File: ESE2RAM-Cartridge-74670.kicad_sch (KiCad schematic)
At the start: 27 parts, among them IC1 4M SRAM, IC2 4M SRAM, J1 BUS_MSX, J2 8M, U1 74HC670, U2 74HC670, U3 74HC138, U4 74HC00, U5 74HC32

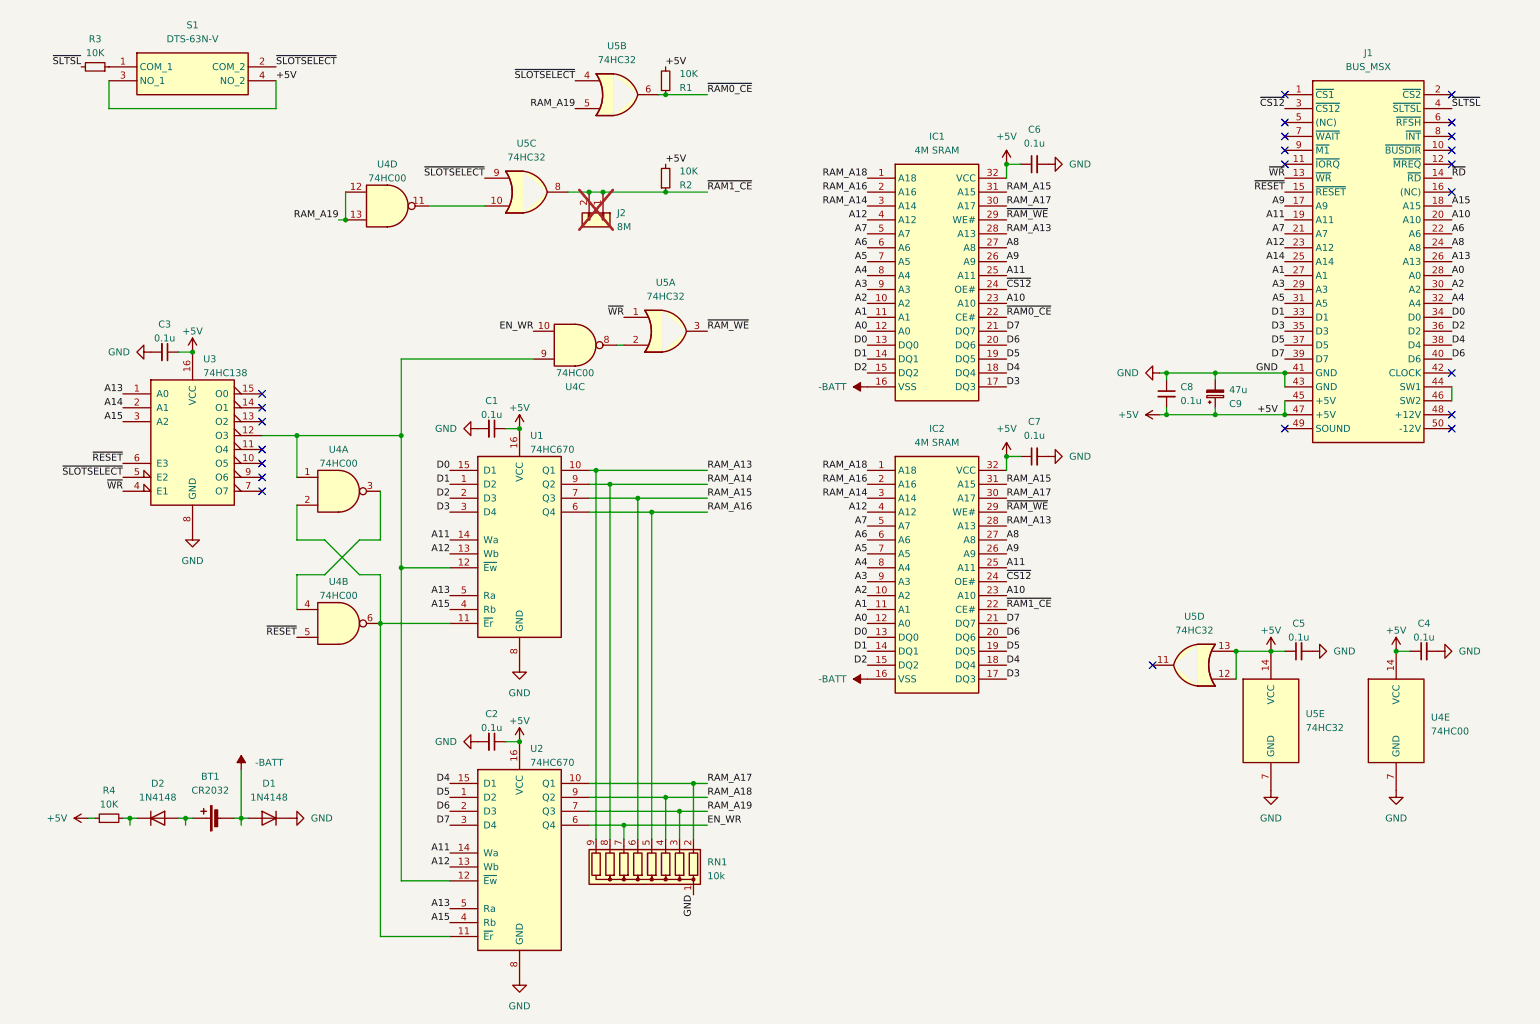
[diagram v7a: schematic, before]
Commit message: Modified Schematic
一部MSX機種での動作不良修正のため74HC00/74HC32/74HC138を74AHCシリーズに変更
Changed 74HC00/74HC32/74HC138 to 74AHC series to fix malfunction on some MSX models.
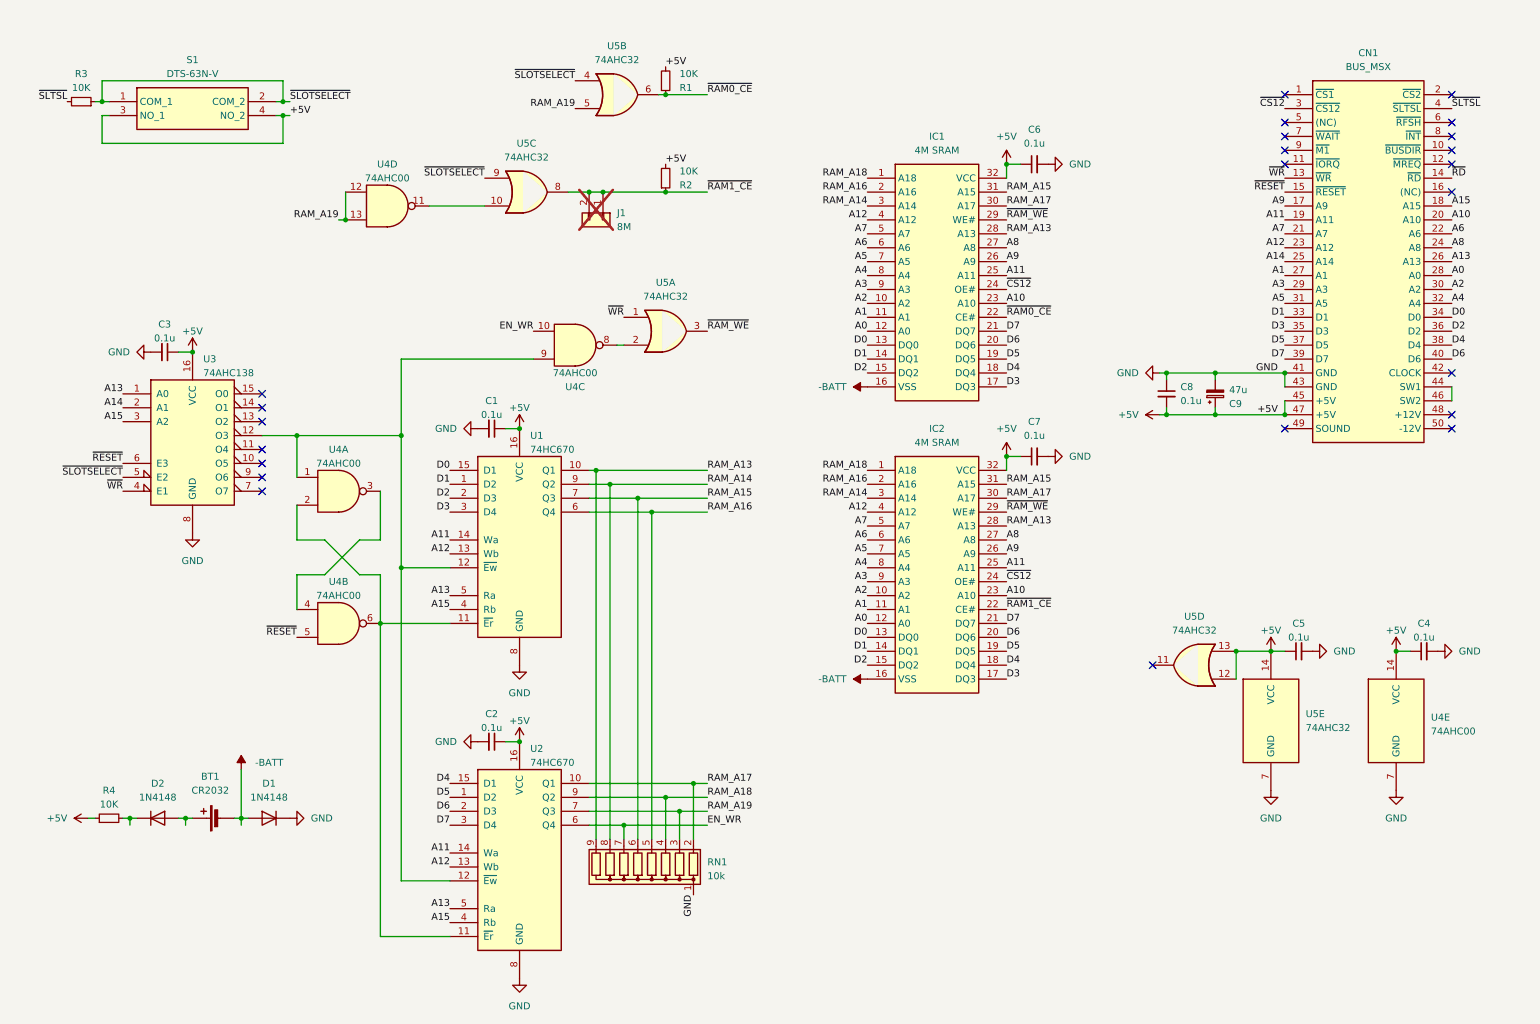
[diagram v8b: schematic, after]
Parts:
- U3: value 74HC138 -> 74AHC138
- U4: value 74HC00 -> 74AHC00
- U5: value 74HC32 -> 74AHC32
- renumbered J1 to CN1, J2 to J1
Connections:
- net ~{SLOTSELECT}: now also R3.1, S1.1 (COM_1)
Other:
- moved on the sheet: R3, S1
